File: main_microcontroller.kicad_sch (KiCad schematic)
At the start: 15 parts, among them SW1 SW_Push, SW2 SW_Push

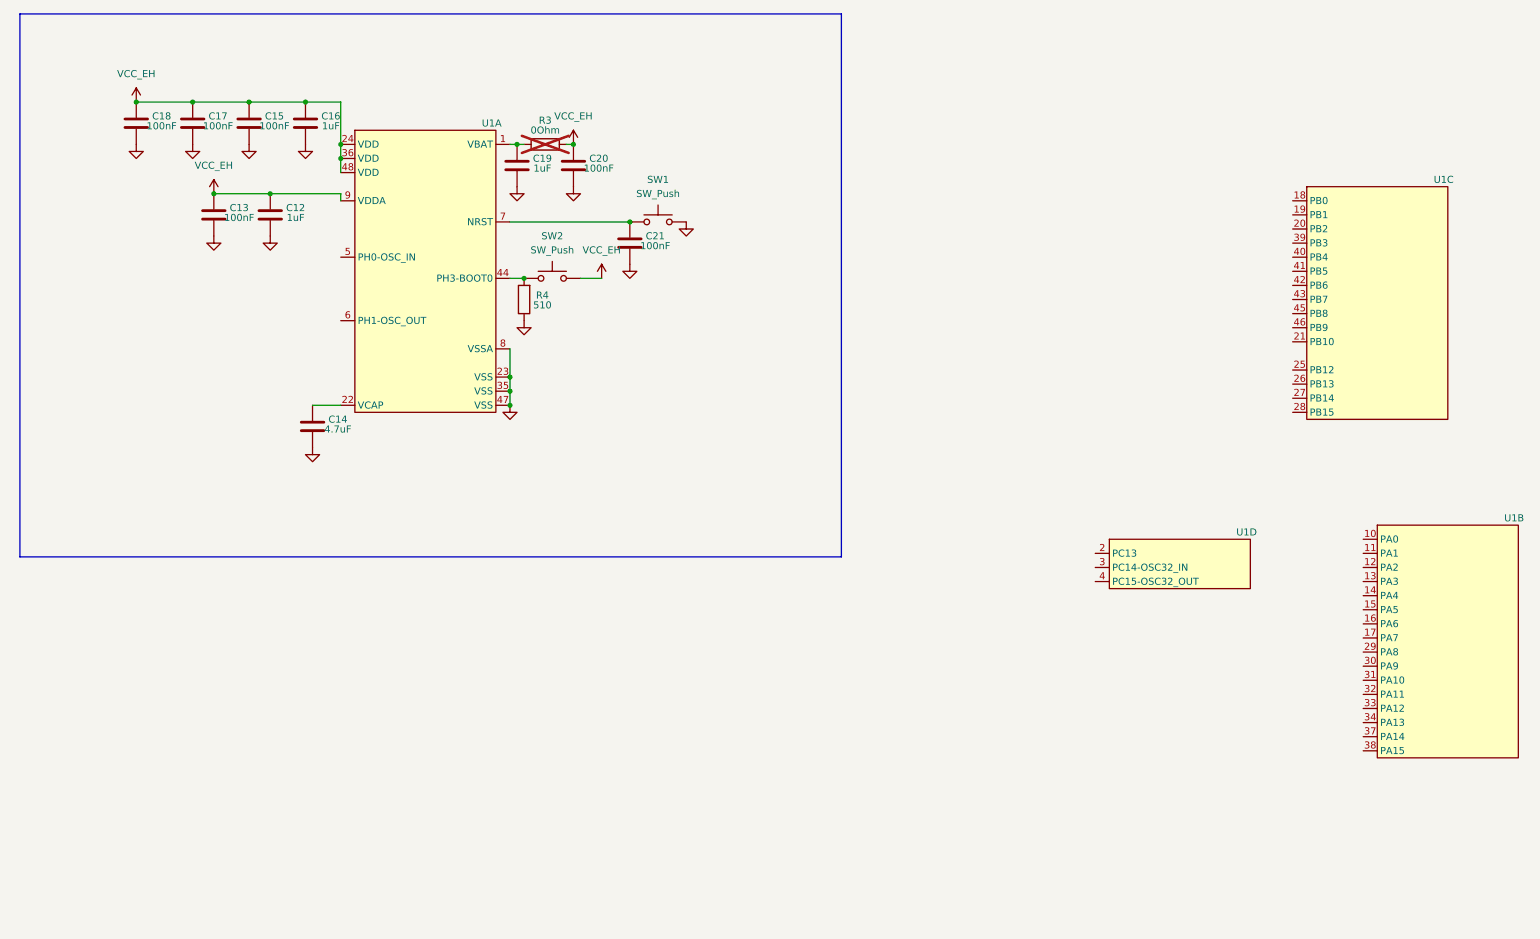
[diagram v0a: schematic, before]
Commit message: changed the mcu to Q version to make use of its SMPS
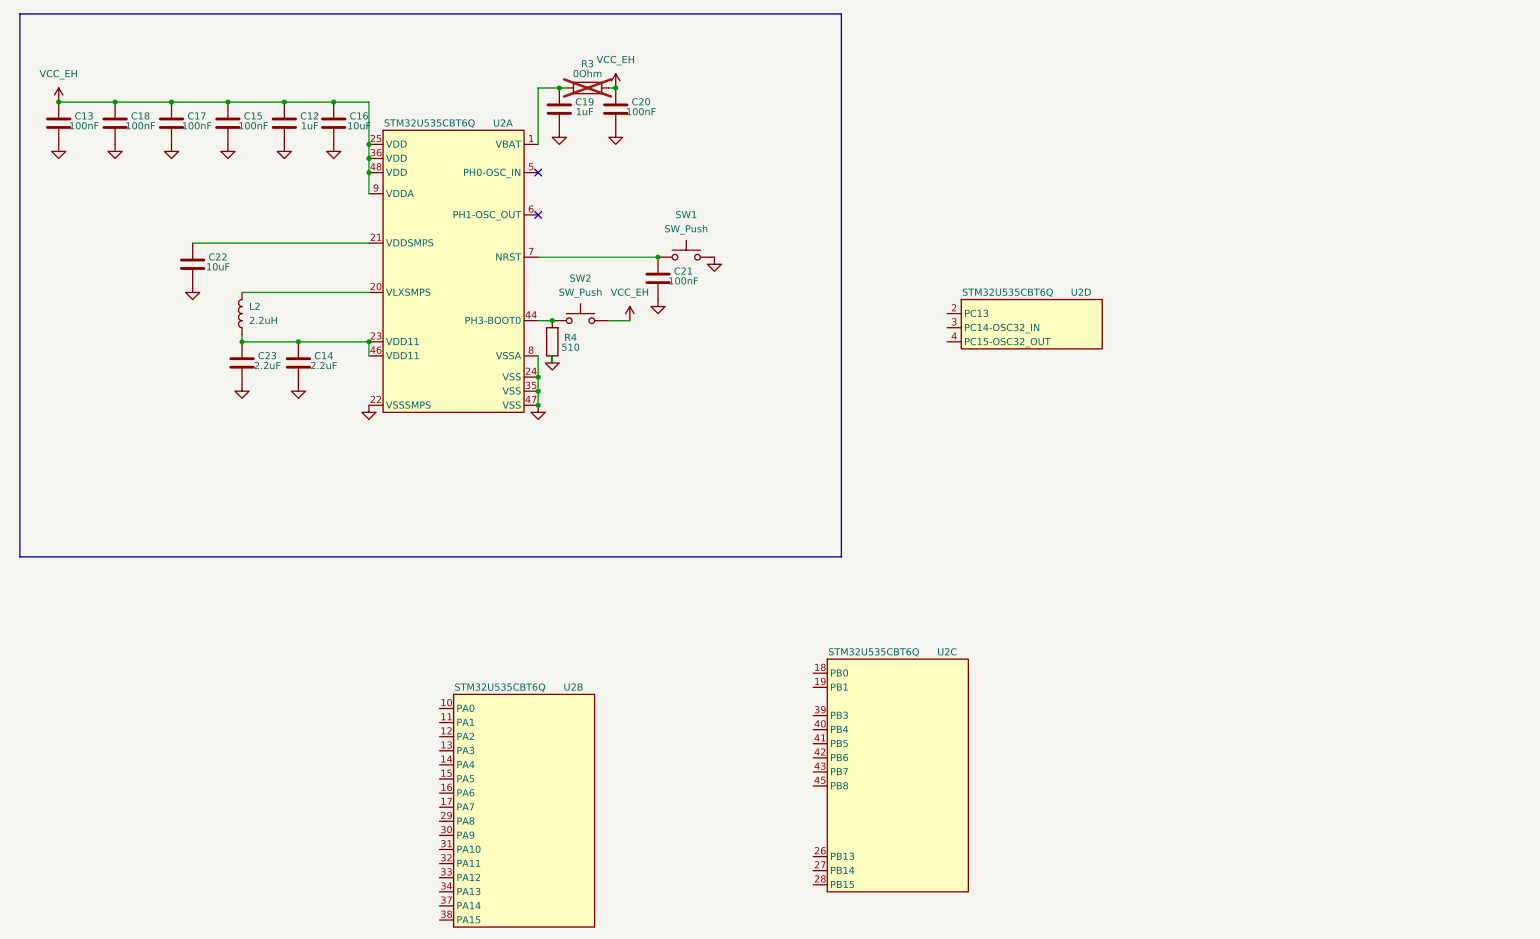
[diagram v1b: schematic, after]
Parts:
- removed U1: (no value), symbol symbols:STM32U535CCT6
- added C22: 10uF, symbol Device:C
- added C23: 2.2uF, symbol Device:C
- added L2: 2.2uH, symbol Device:L
- added U2: STM32U535CBT6Q, symbol symbols:STM32U535CBT6Q
- C14: value 4.7uF -> 2.2uF
- C16: value 1uF -> 10uF
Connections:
- net GND: now also C22.1, C23.1, U2.22 (VSSSMPS), U2.24 (VSS), U2.35 (VSS), U2.47 (VSS), U2.8 (VSSA)
- net VCC_EH: now also U2.25 (VDD), U2.36 (VDD), U2.48 (VDD), U2.9 (VDDA)
- net at C14.2: now also C23.2, L2.1, U2.23 (VDD11), U2.46 (VDD11)
- net at C19.2, R3.1: now also U2.1 (VBAT)
- net at R4.2, SW2.1: now also U2.44 (PH3-BOOT0)
- net at C21.2, SW1.1: now also U2.7 (NRST)
- new net: C22.2, U2.21 (VDDSMPS)
- new net: L2.2, U2.20 (VLXSMPS)
- no-connect marks 0 -> 2
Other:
- moved on the sheet: C12, C13, C14, C15, C16, C17, C18, C19, C20, C21, R3, R4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

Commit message: added ST25DV64KC-IE6T3
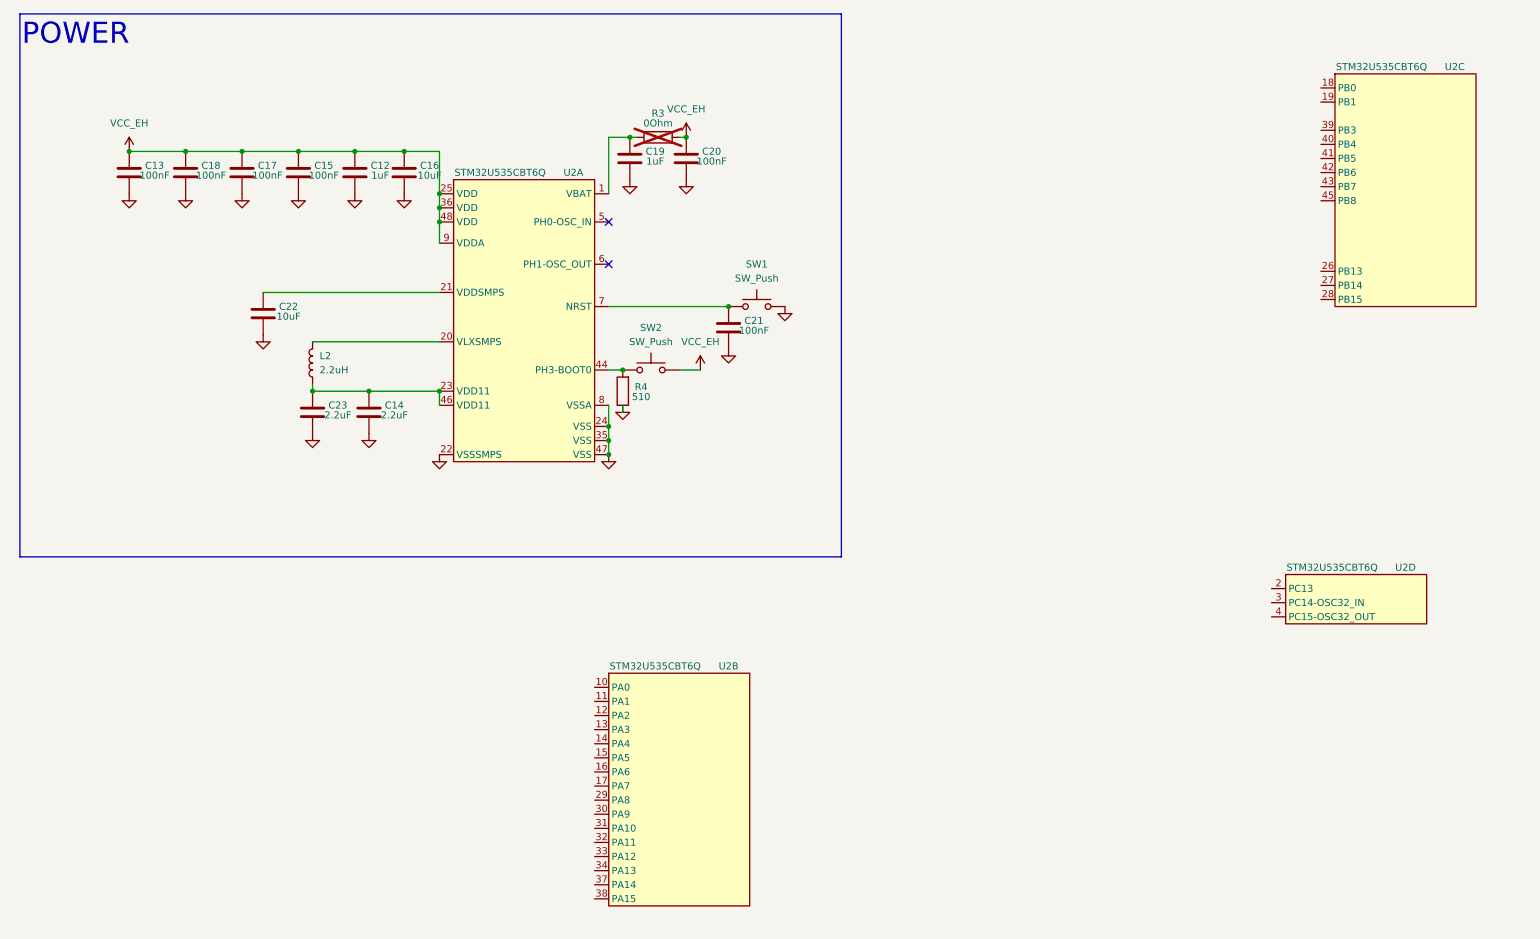
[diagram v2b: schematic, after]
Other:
- note added: "POWER"
- moved on the sheet: C12, C13, C14, C15, C16, C17, C18, C19, C20, C21, C22, C23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
